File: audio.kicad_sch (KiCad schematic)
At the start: 36 parts, among them IC10 LM386

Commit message: prepare for fabrication
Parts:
- C124, C79, C89: LCSC (none) -> C344201; LCSC Part (none) -> C344201
- C225, C226: LCSC (none) -> C83170; LCSC Part (none) -> C83170
- C69: LCSC (none) -> C107154; LCSC Part (none) -> C107154
- IC10: LCSC (none) -> C201575; LCSC Part (none) -> C201575
- R212: LCSC (none) -> C2930266; LCSC Part (none) -> C2930266
- R51, R68: LCSC (none) -> C2907250; LCSC Part (none) -> C2907250
- R65, R66, R81: LCSC (none) -> C2907326; LCSC Part (none) -> C2907326
- R69: LCSC (none) -> C96347; LCSC Part (none) -> C96347
- R82: LCSC (none) -> C17630; LCSC Part (none) -> C17630
- R95: LCSC (none) -> C17408; LCSC Part (none) -> C17408
- R96: LCSC (none) -> C17560; LCSC Part (none) -> C17560
- TP15: now not fitted

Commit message: fix power domains
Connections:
- net +5C: no longer C62.1, C79.2, IM2.16 (Pin_16)
- net +5V: now also C62.1, C79.2, IM2.16 (Pin_16)
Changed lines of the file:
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@@
+	)
+	(junction
+		(at 172.72 71.12)
+		(diameter 0)
+		(color 0 0 0 0)
 	)
 	(junction
@@
 	(junction
 		(at 111.76 95.25)
-		(diameter 0)
-		(color 0 0 0 0)
-	)
-	(junction
-		(at 172.72 71.12)
 		(diameter 0)
 		(color 0 0 0 0)
@@
 	)
 	(symbol
-		(lib_id "power:+5C")
-		(at 172.72 71.12 0)
-		(unit 1)
-		(exclude_from_sim no)
-		(in_bom yes)
-		(on_board yes)
-		(dnp no)
-		(fields_autoplaced yes)
-		(property "Reference" "#PWR0180"
-			(at 172.72 74.93 0)
-			(effects
-				(font
-					(size 1.27 1.27)
-				)
-				(hide yes)
-			)
-		)
-		(property "Value" "+5C"
-			(at 172.72 66.04 0)
-			(effects
-				(font
-					(size 1.27 1.27)
-				)
-			)
-		)
-		(property "Footprint" ""
-			(at 172.72 71.12 0)
-			(effects
-				(font
-					(size 1.27 1.27)
-				)
-				(hide yes)
-			)
-		)
-		(property "Datasheet" ""
-			(at 172.72 71.12 0)
-			(effects
-				(font
-					(size 1.27 1.27)
-				)
-				(hide yes)
-			)
-		)
-		(property "Description" "Power symbol creates a global label with name \"+5C\""
-			(at 172.72 71.12 0)
-			(effects
-				(font
-					(size 1.27 1.27)
-				)
-				(hide yes)
-			)
-		)
-		(pin "1"
-		)
-		(instances
-			(project "Acorn-A3010"
-				(path "/999882f3-94f8-4a89-9093-27a47d0cb289/0f9e4e4c-7eae-43dc-ad37-0c70003f4236"
-					(reference "#PWR0180")
-					(unit 1)
-				)
-			)
-		)
-	)
-	(symbol
 		(lib_id "Device:C_Small")
 		(at 214.63 48.26 270)
@@
 					(unit 1)
 				)
+			)
+		)
+	)
+	(symbol
+		(lib_id "power:+5V")
+		(at 172.72 71.12 0)
+		(unit 1)
+		(exclude_from_sim no)
+		(in_bom yes)
+		(on_board yes)
+		(dnp no)
+		(fields_autoplaced yes)
+		(property "Reference" "#PWR0292"
+			(at 172.72 74.93 0)
+			(effects
+				(font
+					(size 1.27 1.27)
+				)
+				(hide yes)
+			)
+		)
+		(property "Value" "+5V"
+			(at 172.7201 67.31 90)
+			(effects
+				(font
+					(size 1.27 1.27)
+				)
+				(justify left)
+			)
+		)
+		(property "Footprint" ""
+			(at 172.72 71.12 0)
+			(effects
+				(font
+					(size 1.27 1.27)
+				)
+				(hide yes)
+			)
+		)
+		(property "Datasheet" ""
+			(at 172.72 71.12 0)
+			(effects
+				(font
+					(size 1.27 1.27)
+				)
+				(hide yes)
+			)
+		)
+		(property "Description" "Power symbol creates a global label with name \"+5V\""
+			(at 172.72 71.12 0)
+			(effects
+				(font
+					(size 1.27 1.27)
+				)
+				(hide yes)
+			)
+		)
+		(pin "1"
+		)
+		(instances
+			(project "Acorn-A3010"
+				(path "/999882f3-94f8-4a89-9093-27a47d0cb289/0f9e4e4c-7eae-43dc-ad37-0c70003f4236"
+					(reference "#PWR0292")
+					(unit 1)
+				)

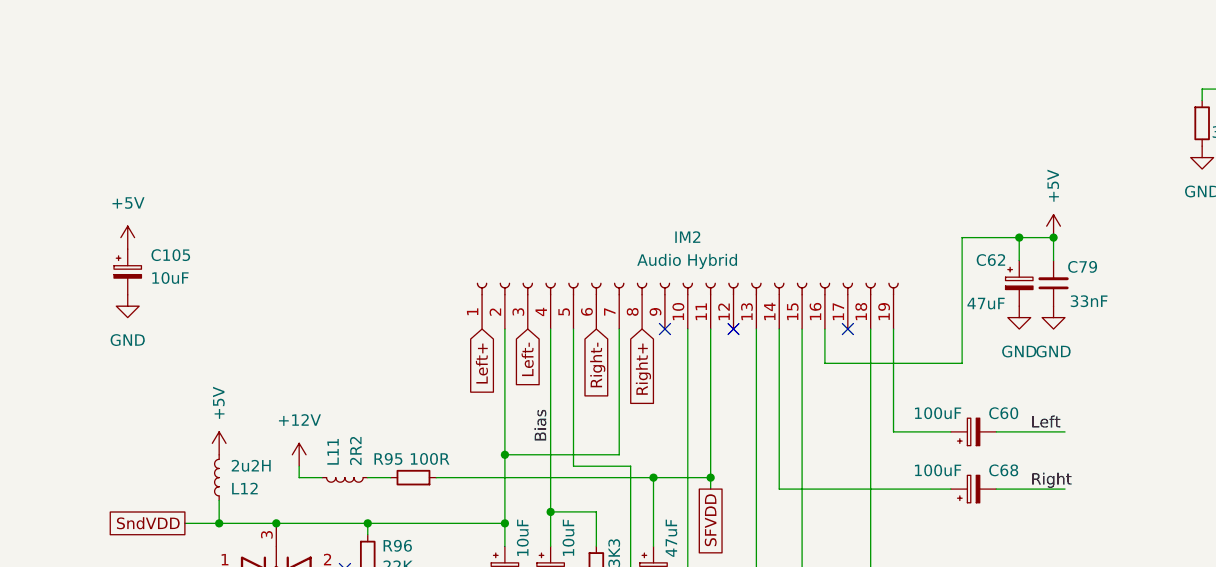
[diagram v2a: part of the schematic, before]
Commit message: split power domain on board to separate 5C
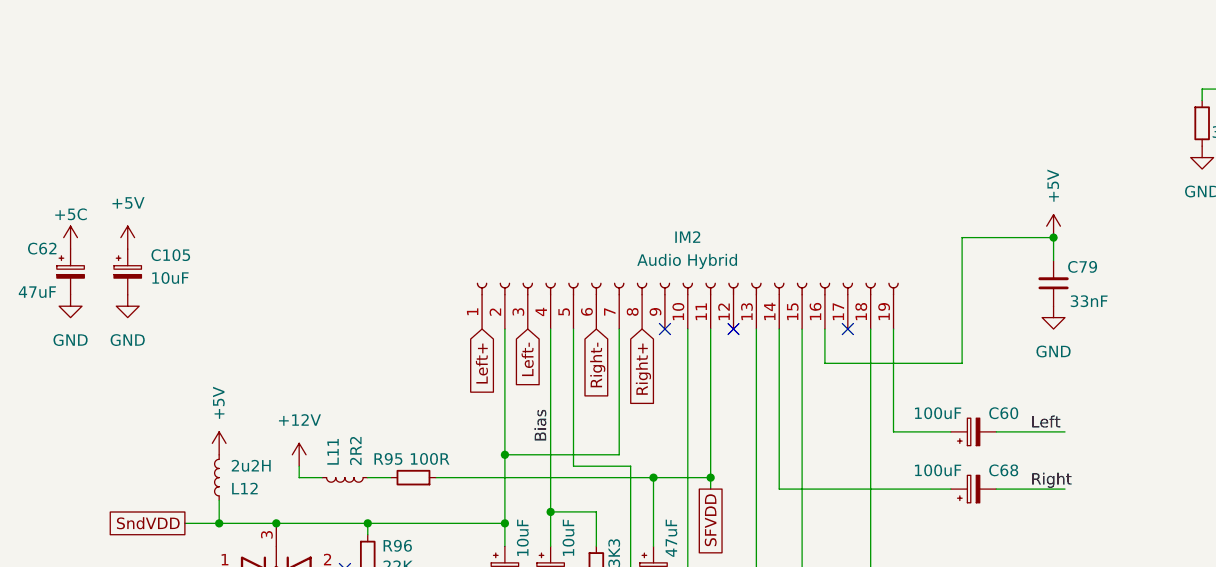
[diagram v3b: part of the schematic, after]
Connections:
- net +5C: now also C62.1
- net +5V: no longer C62.1
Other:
- moved on the sheet: C62
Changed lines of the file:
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@@
 	)
 	(junction
-		(at 168.91 71.12)
-		(diameter 0)
-		(color 0 0 0 0)
-	)
-	(junction
 		(at 86.36 102.87)
 		(diameter 0)
@@
 	(wire
 		(pts
-			(xy 162.56 71.12) (xy 168.91 71.12)
-		)
-		(stroke
-			(width 0)
-			(type default)
-		)
-	)
-	(wire
-		(pts
 			(xy 241.3 44.45) (xy 241.3 57.15)
 		)
@@
 	(wire
 		(pts
-			(xy 168.91 71.12) (xy 168.91 73.66)
-		)
-		(stroke
-			(width 0)
-			(type default)
-		)
-	)
-	(wire
-		(pts
 			(xy 237.49 100.33) (xy 237.49 111.76)
 		)
@@
 	(wire
 		(pts
-			(xy 168.91 71.12) (xy 172.72 71.12)
+			(xy 162.56 71.12) (xy 172.72 71.12)
 		)
 		(stroke
@@
 	(symbol
 		(lib_id "Device:C_Polarized_Small")
-		(at 168.91 76.2 0)
+		(at 63.5 74.93 0)
 		(unit 1)
 		(exclude_from_sim no)
@@
 		(dnp no)
 		(property "Reference" "C62"
-			(at 164.084 73.66 0)
+			(at 58.674 72.39 0)
 			(effects
 				(font
@@
 		)
 		(property "Value" "47uF"
-			(at 163.068 78.486 0)
+			(at 57.658 77.216 0)
 			(effects
 				(font
@@
 		)
 		(property "Footprint" "Capacitor_THT:CP_Radial_D8.0mm_P5.00mm"
-			(at 168.91 76.2 0)
+			(at 63.5 74.93 0)
 			(effects
 				(font
@@
 		)
 		(property "Datasheet" "~"
-			(at 168.91 76.2 0)
+			(at 63.5 74.93 0)
 			(effects
 				(font
@@
 		)
 		(property "Description" "Polarized capacitor, small symbol"
-			(at 168.91 76.2 0)
+			(at 63.5 74.93 0)
 			(effects
 				(font
@@
 	)
 	(symbol
+		(lib_id "power:+5C")
+		(at 63.5 72.39 0)
+		(unit 1)
+		(exclude_from_sim no)
+		(in_bom yes)
+		(on_board yes)
+		(dnp no)
+		(property "Reference" "#PWR0180"
+			(at 63.5 76.2 0)
+			(effects
+				(font
+					(size 1.27 1.27)
+				)
+				(hide yes)
+			)
+		)
+		(property "Value" "+5C"
+			(at 63.5 68.58 0)
+			(effects
+				(font
+					(size 1.27 1.27)
+				)
+			)
+		)
+		(property "Footprint" ""
+			(at 63.5 72.39 0)
+			(effects
+				(font
+					(size 1.27 1.27)
+				)
+				(hide yes)
+			)
+		)
+		(property "Datasheet" ""
+			(at 63.5 72.39 0)
+			(effects
+				(font
+					(size 1.27 1.27)
+				)
+				(hide yes)
+			)
+		)
+		(property "Description" "Power symbol creates a global label with name \"+5C\""
+			(at 63.5 72.39 0)
+			(effects
+				(font
+					(size 1.27 1.27)
+				)
+				(hide yes)
+			)
+		)
+		(pin "1"
+		)
+		(instances
+			(project "Acorn-A3010"
+				(path "/999882f3-94f8-4a89-9093-27a47d0cb289/0f9e4e4c-7eae-43dc-ad37-0c70003f4236"
+					(reference "#PWR0180")
+					(unit 1)
+				)
+			)
+		)
+	)
+	(symbol
 		(lib_id "Connector:Conn_01x02_Pin")
 		(at 238.76 39.37 90)
@@
 	(symbol
 		(lib_id "power:GND")
-		(at 168.91 78.74 0)
+		(at 63.5 77.47 0)
 		(unit 1)
 		(exclude_from_sim no)
@@
 		(fields_autoplaced yes)
 		(property "Reference" "#PWR0181"
-			(at 168.91 85.09 0)
+			(at 63.5 83.82 0)
 			(effects
 				(font
@@
 		)
 		(property "Value" "GND"
-			(at 168.91 83.82 0)
+			(at 63.5 82.55 0)
 			(effects
 				(font
@@
 		)
 		(property "Footprint" ""
-			(at 168.91 78.74 0)
+			(at 63.5 77.47 0)
 			(effects
 				(font
@@
 		)
 		(property "Datasheet" ""
-			(at 168.91 78.74 0)
+			(at 63.5 77.47 0)
 			(effects
 				(font
@@
 		)
 		(property "Description" "Power symbol creates a global label with name \"GND\" , ground"
-			(at 168.91 78.74 0)
+			(at 63.5 77.47 0)
 			(effects
 				(font
